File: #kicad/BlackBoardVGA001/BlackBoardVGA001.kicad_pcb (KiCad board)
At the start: 2 copper layers, 72.5 x 85.1 mm, 30 parts, among them J1 VGA, J2 PS/2, J3 Left, J4 Right, J5 LAN8720, J6 PS/2

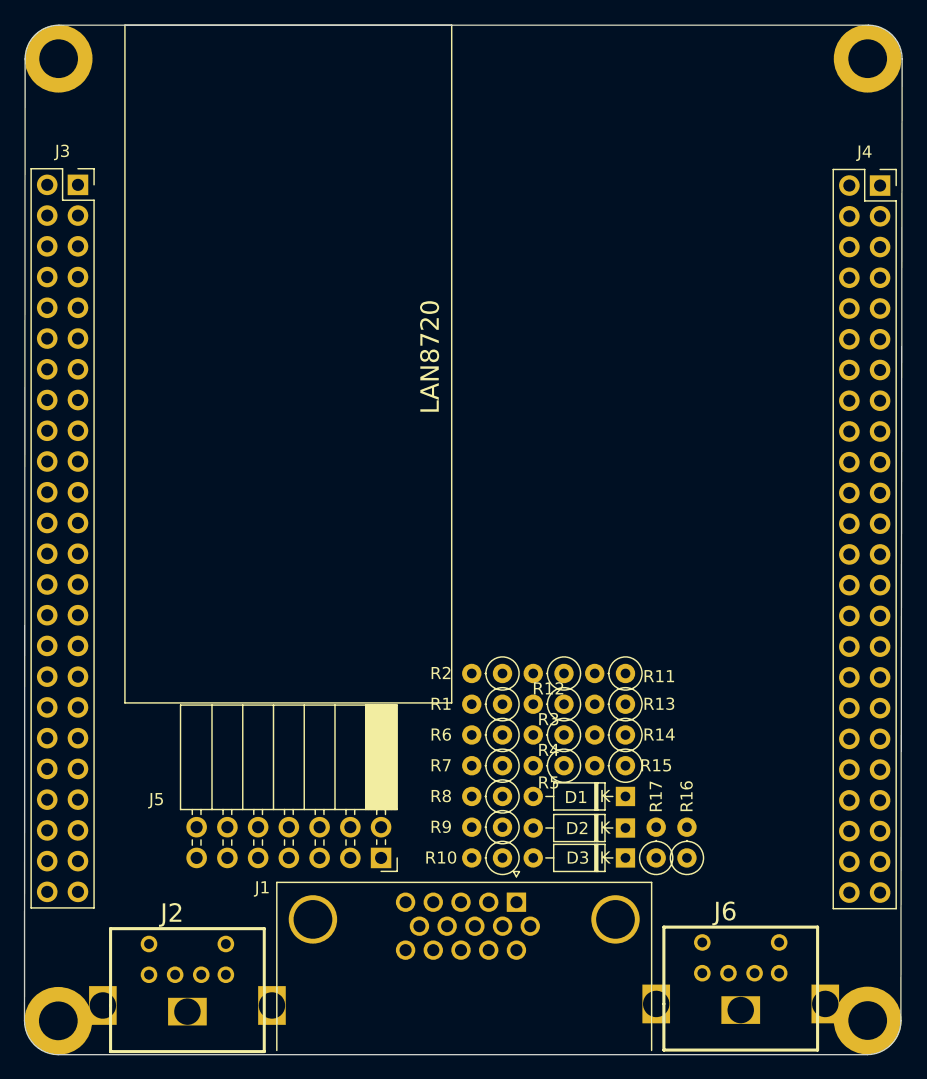
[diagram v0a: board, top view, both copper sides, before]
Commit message: moved VGA connector to other end of board
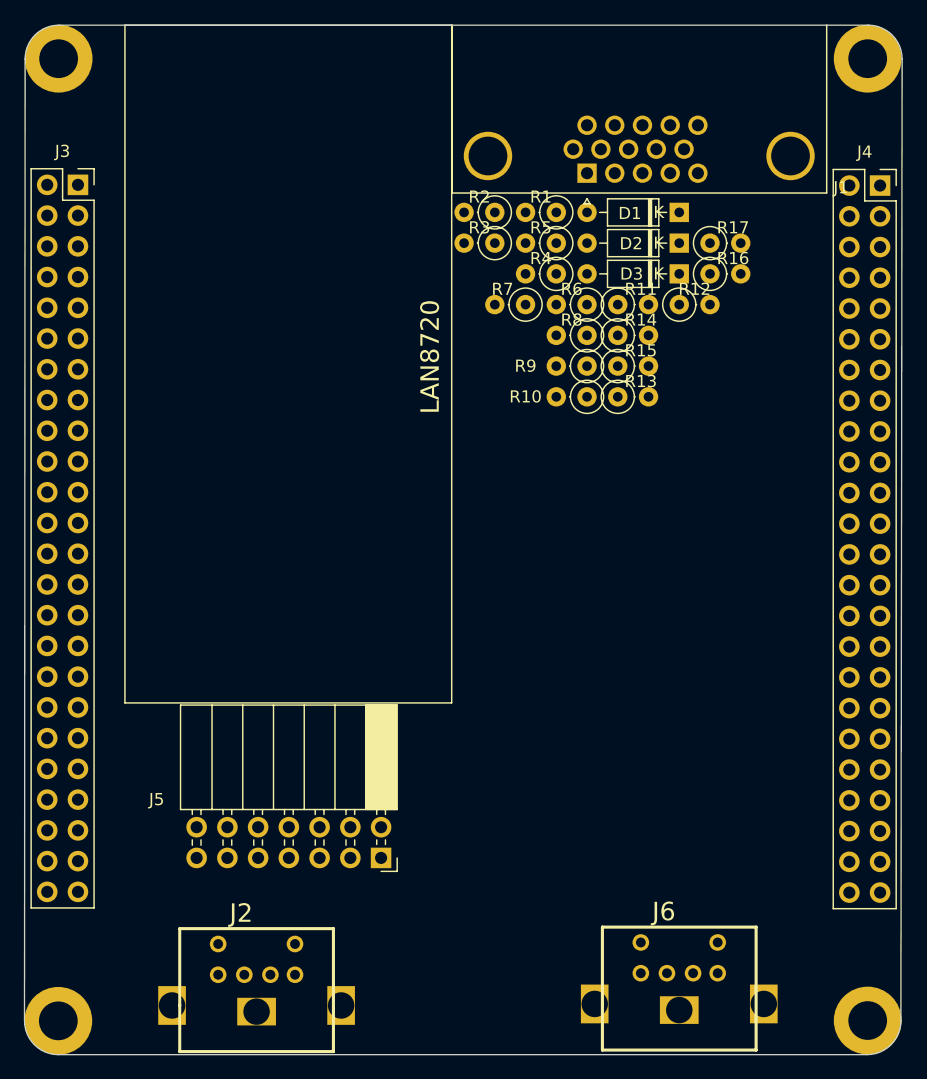
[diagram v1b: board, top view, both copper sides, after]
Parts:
- moved J1 60.5 mm to (87.6, 70.4), turned to 180 degrees
- moved R17 51.0 mm to (97.8, 76.2), turned to 0 degrees
- moved D2 48.5 mm to (95.2, 76.2)
- moved D1 48.5 mm to (95.2, 73.7)
- moved D3 48.5 mm to (95.2, 78.7)
- moved R16 48.3 mm to (97.8, 78.7), turned to 0 degrees
- moved R5 43.2 mm to (85.1, 76.2)
- moved R1 40.9 mm to (85.1, 73.7)
- moved R8 38.7 mm to (87.6, 83.8)
- moved R10 38.7 mm to (87.6, 88.9)
- moved R9 38.7 mm to (87.6, 86.4)
- moved R3 38.5 mm to (80.0, 76.2)
- moved R7 38.1 mm to (82.5, 81.3)
- moved R2 38.1 mm to (80.0, 73.7)
- moved R4 38.1 mm to (85.1, 78.7)
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
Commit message: using E0 and E1 for second PS/2
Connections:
- J6 pad 1: Net-(J6-Pad1) -> PE1
- J6 pad 5: Net-(J6-Pad5) -> PE0

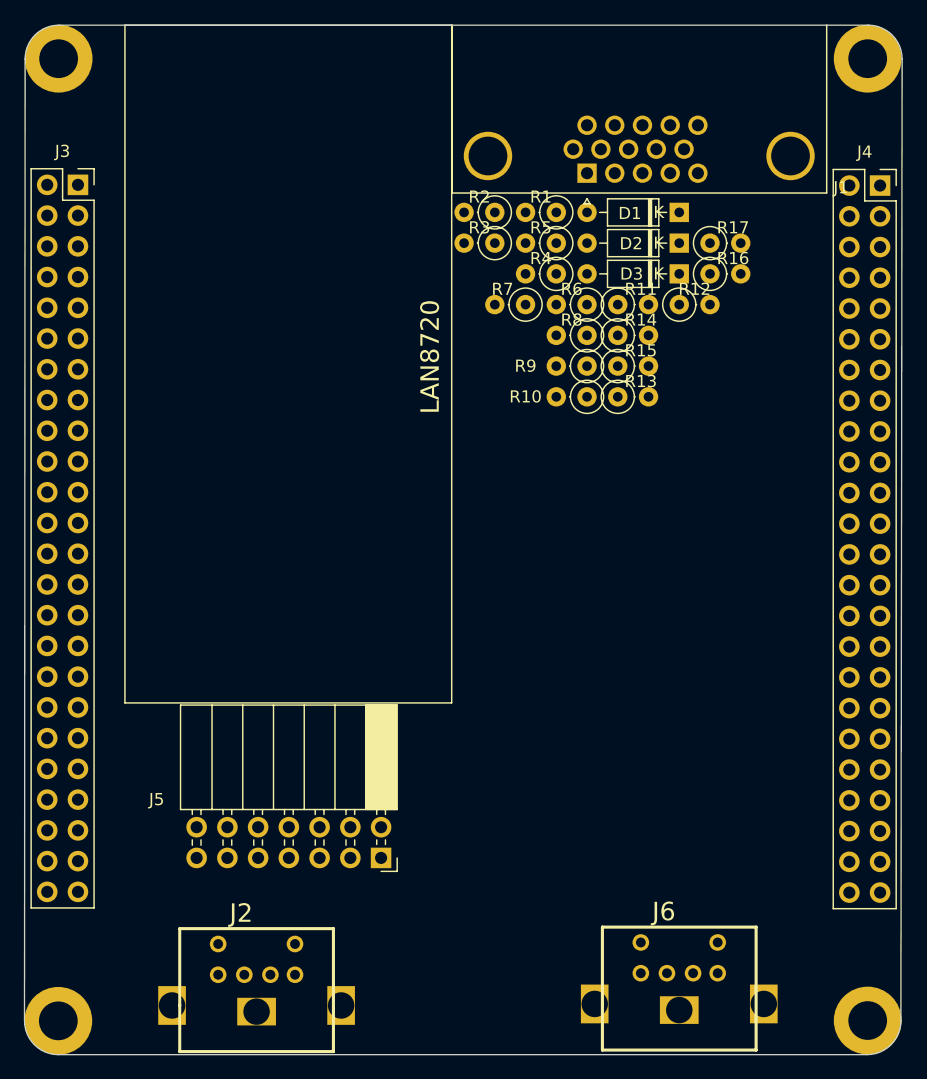
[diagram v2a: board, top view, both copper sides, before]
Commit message: swap position of LAN8720 and VGA
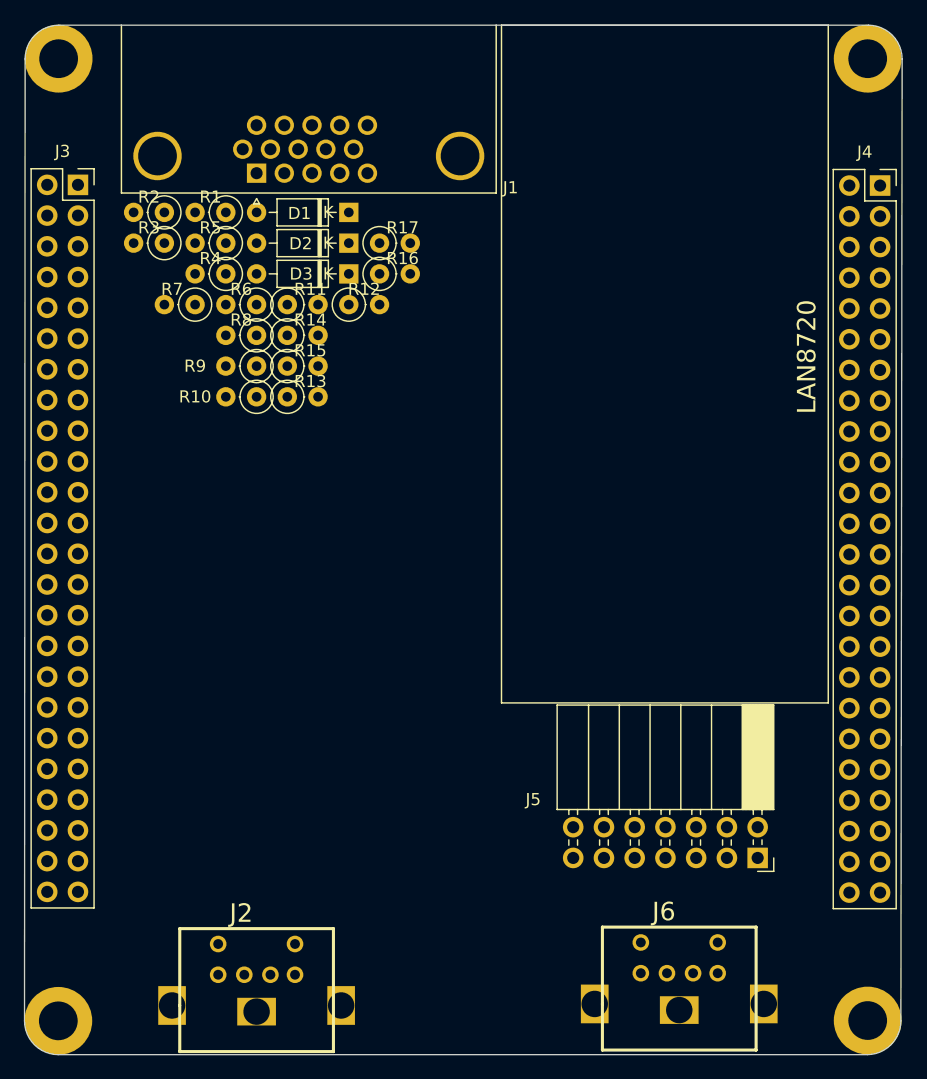
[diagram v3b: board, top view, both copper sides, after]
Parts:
- moved J5 31.1 mm to (101.7, 127.0)
- moved D1 27.3 mm to (67.9, 73.7)
- moved D2 27.3 mm to (67.9, 76.2)
- moved D3 27.3 mm to (67.9, 78.7)
- moved R1 27.3 mm to (57.8, 73.7)
- moved R12 27.3 mm to (67.9, 81.3)
- moved R16 27.3 mm to (70.5, 78.7)
- moved R17 27.3 mm to (70.5, 76.2)
- moved R2 27.3 mm to (52.7, 73.7)
- moved R3 27.3 mm to (52.7, 76.2)
- moved R4 27.3 mm to (57.8, 78.7)
- moved R5 27.3 mm to (57.8, 76.2)
- moved R11 27.3 mm to (62.9, 81.3)
- moved R13 27.3 mm to (62.9, 88.9)
- moved R14 27.3 mm to (62.9, 83.8)
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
